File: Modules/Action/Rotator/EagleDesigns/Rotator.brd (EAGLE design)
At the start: 100 x 80 mm, 9 parts, among them U2 ATMEGA328P_TQFP

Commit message: Revert "Merge branch 'version-1.2'"
This reverts commit 982d9c85d5bd00c48b539e840003de48d3cf178d, reversing
changes made to b3895ae538c161df72313035d3e956c7a5ec4dbc.
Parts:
- removed C1, C2: 22pF, adafruit:C0603
- removed R2: 10K, resistor:R0603
- removed U$2: NX503, MakerWear:NX503
- removed U2: ATMEGA328P_TQFP, SparkFun-DigitalIC:TQFP32-08
- added U1: TINY85-20-DIP, SparkFun-DigitalIC:DIP08
- JP2: device SparkFun-Connectors:1X03 -> SparkFun-Connectors:1X04
- moved R1 14.8 mm to (4.58, 12.0), turned to 270 degrees
- moved JP3 3.74 mm to (20.7, 9.56), turned to 90 degrees
- moved JP1 1.66 mm to (17.2, 3.89)
- moved JP2 0.31 mm to (9.46, 20.2)
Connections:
- removed net 1X3SIN: U2.23
- removed net N$1: C1.1, U$2.P$1, U2.7
- removed net N$3: C2.1, U$2.P$2, U2.8
- removed net RESET: JP2.1, R2.1, U2.29
- removed net RX: JP2.2, U2.30
- removed net TX: JP2.3, U2.31
- new net MOSI: JP2.2, U1.5
- new net NRES: JP2.1, U1.1
- new net OUT(MISO): JP2.3, JP3.1, U1.6
- new net SCK: JP2.4, U1.7
- net 1X3SIN-SOUT: now also U1.2
- net GND: now also U1.4; no longer C1.2, C2.2, U2.21, U2.3, U2.5
- net VCC: now also U1.8; no longer R2.2, U2.18, U2.4, U2.6
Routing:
- net NRES: track 0.00 -> 22.7 mm
- net OUT(MISO): track 0.00 -> 20.6 mm
- net N$1: track 20.6 -> 0.00 mm, vias 1 -> 0
- net VCC: track 43.5 -> 23.4 mm, vias 1 -> 0
- net N$3: track 15.8 -> 0.00 mm, vias 1 -> 0
- net RESET: track 13.5 -> 0.00 mm
- net 1X3SIN-SOUT: track 14.4 -> 23.9 mm
- net SCK: track 0.00 -> 6.58 mm
- net GND: track 40.9 -> 34.5 mm, vias 1 -> 0
- net MOSI: track 0.00 -> 6.23 mm
- net TX: track 5.62 -> 0.00 mm
- net RX: track 3.94 -> 0.00 mm
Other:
- outline, holes or cut-outs redrawn
- board text added: "CTRL"
- board text added: "MISO"
- board text added: "MOSI"
- board text added: "MW-V3"
- board text added: "NRES"
- board text added: "SCK"
- board text added: "Servo Motor"
- board text added: "VCC"
- board text removed: "ROTATOR"

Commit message: added Rotator #30 eagle files
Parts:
- removed U1: TINY85-20-DIP, SparkFun-DigitalIC:DIP08
- added C1, C2: 22pF, adafruit:C0603
- added R2: 10K, resistor:R0603
- added U$2: NX503, MakerWear:NX503
- added U2: ATMEGA328P_TQFP, SparkFun-DigitalIC:TQFP32-08
- JP2: device SparkFun-Connectors:1X04 -> SparkFun-Connectors:1X03
- moved R1 14.8 mm to (17.7, 5.16), turned to 180 degrees
- moved JP3 3.74 mm to (19.9, 13.2), turned to 270 degrees
- moved JP1 1.66 mm to (16.0, 2.66)
- moved JP2 0.31 mm to (9.68, 20.4)
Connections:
- removed net MOSI: JP2.2, U1.5
- removed net NRES: JP2.1, U1.1
- removed net OUT(MISO): JP2.3, JP3.1, U1.6
- removed net SCK: JP2.4, U1.7
- new net 1X3SIN: U2.23
- new net N$1: C1.1, U$2.P$1, U2.7
- new net N$3: C2.1, U$2.P$2, U2.8
- new net RESET: JP2.1, R2.1, U2.29
- new net RX: JP2.2, U2.30
- new net TX: JP2.3, U2.31
- net 1X3SIN-SOUT: no longer U1.2
- net GND: now also C1.2, C2.2, U2.21, U2.3, U2.5; no longer U1.4
- net VCC: now also R2.2, U2.18, U2.4, U2.6; no longer U1.8
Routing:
- net NRES: track 22.7 -> 0.00 mm
- net OUT(MISO): track 20.6 -> 0.00 mm
- net N$1: track 0.00 -> 20.6 mm, vias 0 -> 1
- net VCC: track 23.4 -> 43.5 mm, vias 0 -> 1
- net N$3: track 0.00 -> 15.8 mm, vias 0 -> 1
- net RESET: track 0.00 -> 13.5 mm
- net 1X3SIN-SOUT: track 23.9 -> 14.4 mm
- net SCK: track 6.58 -> 0.00 mm
- net GND: track 34.5 -> 40.9 mm, vias 0 -> 1
- net MOSI: track 6.23 -> 0.00 mm
- net TX: track 0.00 -> 5.62 mm
- net RX: track 0.00 -> 3.94 mm
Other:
- outline, holes or cut-outs redrawn
- board text added: "ROTATOR"
- board text removed: "CTRL"
- board text removed: "MISO"
- board text removed: "MOSI"
- board text removed: "MW-V3"
- board text removed: "NRES"
- board text removed: "SCK"
- board text removed: "Servo Motor"
- board text removed: "VCC"

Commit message: fixed eagle files for new modules
SIN/SOUT was not correctly connected in them.
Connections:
- removed net 1X3SIN: U2.23
- new net SERVO: JP3.1, U2.13
- net 1X3SIN-SOUT: now also U2.23
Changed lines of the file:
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@@
 <wire x1="8.42" y1="4.02" x2="8.7" y2="4.3" width="0.3048" layer="1"/>
 <wire x1="8.7" y1="4.3" x2="15.8" y2="4.3" width="0.3048" layer="1"/>
+<contactref element="U2" pad="23"/>
+<wire x1="8.7" y1="4.3" x2="5.8074" y2="14.54" width="0" layer="19" extent="1-16"/>
 </signal>
 <signal name="RESET">
@@
 <wire x1="14.8" y1="20.15" x2="14.76" y2="20.39" width="0.3048" layer="16"/>
 </signal>
-<signal name="1X3SIN">
-<contactref element="U2" pad="23"/>
-</signal>
 <signal name="N$1">
 <contactref element="U$2" pad="P$1"/>
@@
 <wire x1="8" y1="12.03" x2="7.89" y2="15.04" width="0.3048" layer="1"/>
 </signal>
+<signal name="SERVO">
+<contactref element="U2" pad="13"/>
+<contactref element="JP3" pad="1"/>
+<wire x1="9.7" y1="8.2474" x2="19.89" y2="13.21" width="0" layer="19" extent="16-16"/>
+</signal>
 </signals>

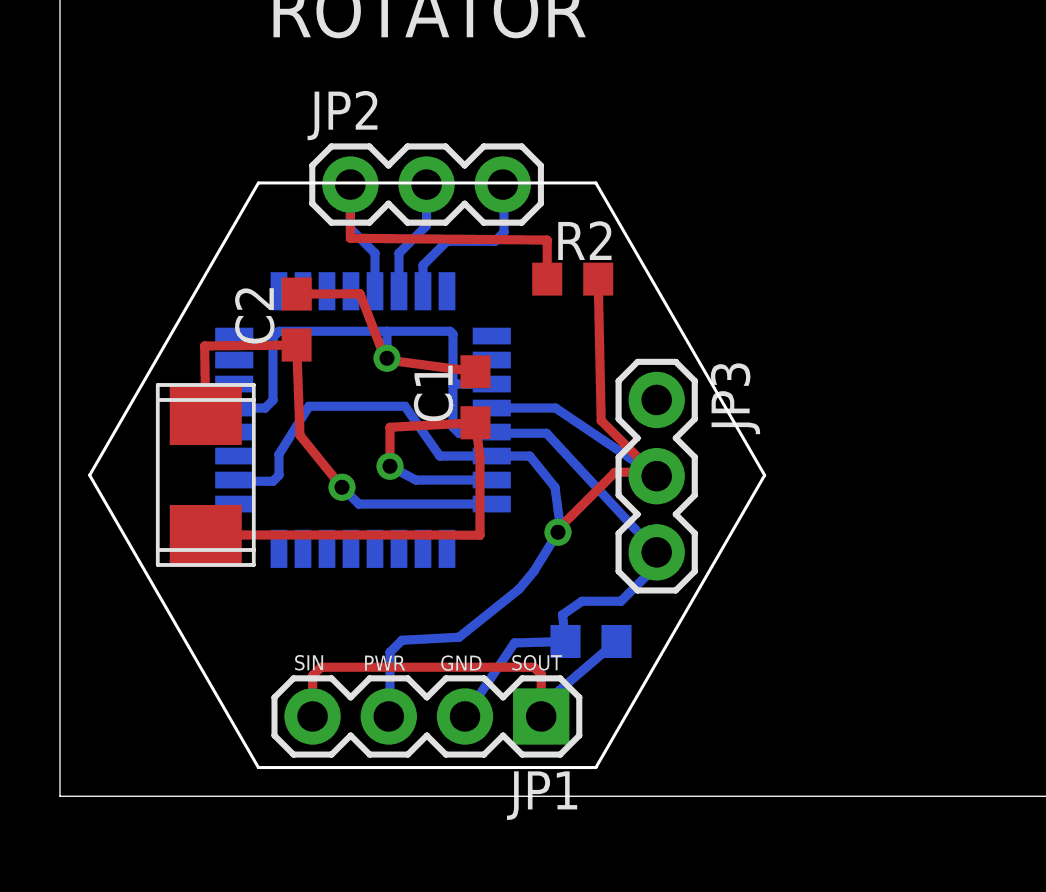
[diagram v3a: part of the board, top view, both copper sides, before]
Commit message: Rotator: added final PCB #30
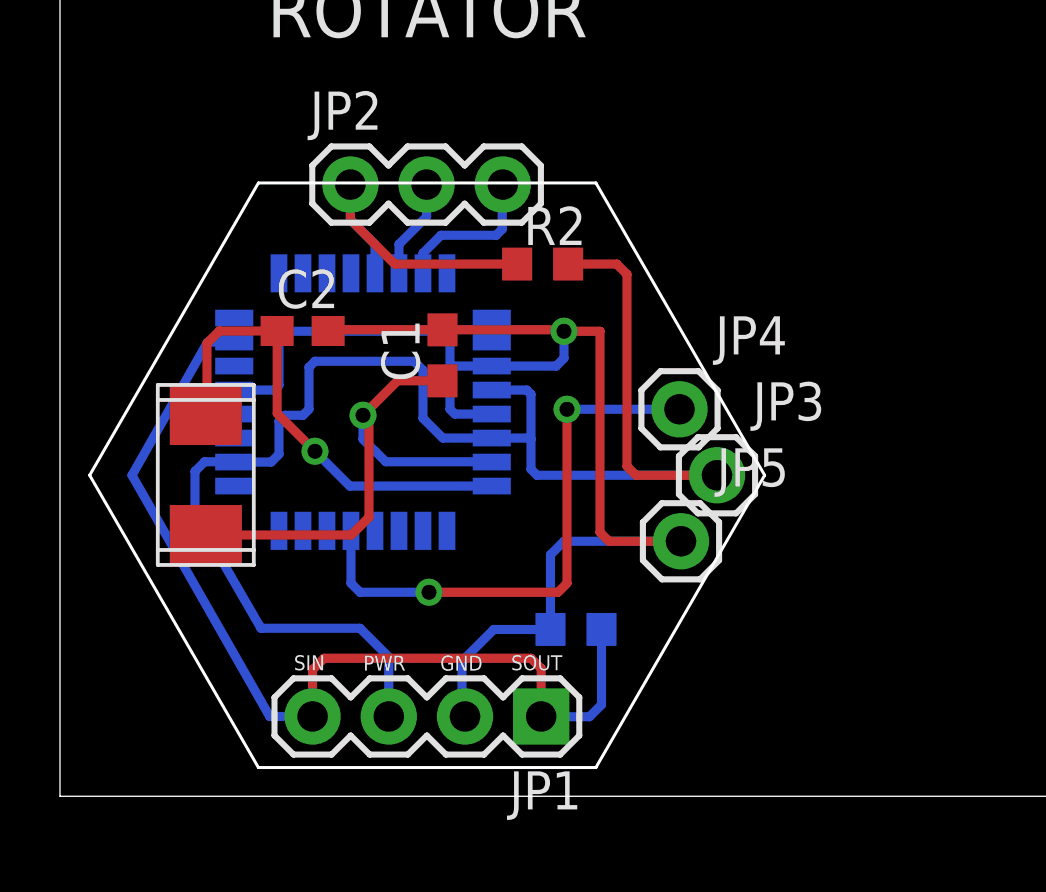
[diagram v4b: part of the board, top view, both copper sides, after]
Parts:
- added JP4, JP5: (no value), SparkFun-Connectors:1X01
- JP3: device SparkFun-Connectors:1X03 -> SparkFun-Connectors:1X01
- moved JP3 3.22 mm to (21.9, 10.7), turned to 0 degrees
- moved C1 1.78 mm to (12.8, 14.7)
- moved R2 1.12 mm to (16.1, 17.7)
- moved R1 0.64 mm to (17.2, 5.56)
- moved U2 0.60 mm to (10.1, 13.1)
- moved C2 0.43 mm to (8.09, 15.5), turned to 0 degrees
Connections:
- net GND: now also JP5.1; no longer JP3.3
- net SERVO: now also JP4.1; no longer JP3.1
- net VCC: now also JP3.1; no longer JP3.2
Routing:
- net SERVO: track 0.00 -> 18.7 mm, vias 0 -> 2
- net 1X3SIN-SOUT: track 14.4 -> 32.4 mm
- net GND: track 40.9 -> 48.5 mm
- net VCC: track 43.5 -> 50.4 mm, vias 1 -> 0
- net RESET: track 13.5 -> 10.6 mm
- net N$1: track 20.6 -> 17.7 mm
- net RX: track 3.94 -> 3.34 mm

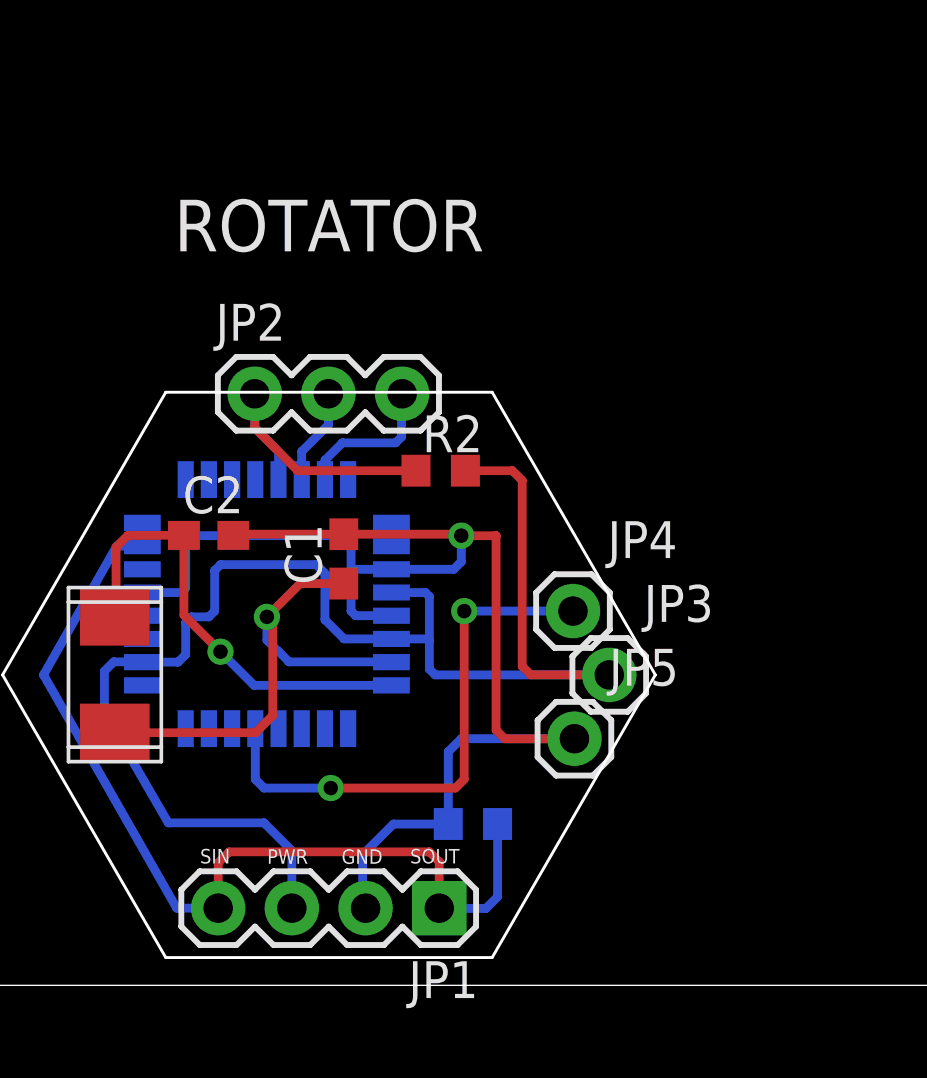
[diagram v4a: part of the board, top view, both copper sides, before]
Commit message: added version numbers, and deleted most of the text that was on each module.
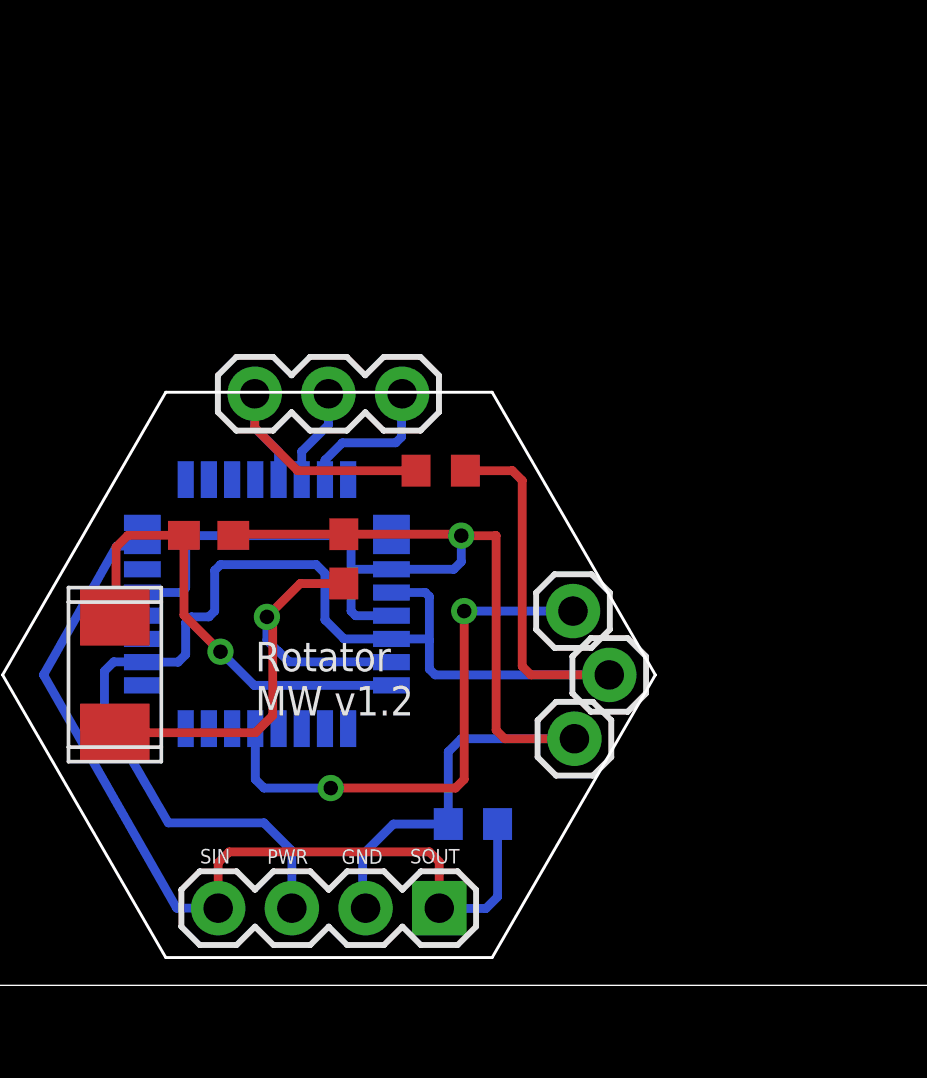
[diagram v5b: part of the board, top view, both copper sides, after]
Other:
- board text added: "Rotator MW v1.2"
- board text removed: "ROTATOR"
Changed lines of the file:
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@@
 <layer number="19" name="Unrouted" color="6" fill="1" visible="yes" active="yes"/>
 <layer number="20" name="Dimension" color="15" fill="1" visible="yes" active="yes"/>
-<layer number="21" name="tPlace" color="7" fill="1" visible="no" active="yes"/>
-<layer number="22" name="bPlace" color="7" fill="1" visible="no" active="yes"/>
+<layer number="21" name="tPlace" color="7" fill="1" visible="yes" active="yes"/>
+<layer number="22" name="bPlace" color="7" fill="1" visible="yes" active="yes"/>
 <layer number="23" name="tOrigins" color="15" fill="1" visible="yes" active="yes"/>
 <layer number="24" name="bOrigins" color="15" fill="1" visible="yes" active="yes"/>
-<layer number="25" name="tNames" color="7" fill="1" visible="no" active="yes"/>
-<layer number="26" name="bNames" color="7" fill="1" visible="no" active="yes"/>
-<layer number="27" name="tValues" color="7" fill="1" visible="no" active="yes"/>
-<layer number="28" name="bValues" color="7" fill="1" visible="no" active="yes"/>
+<layer number="25" name="tNames" color="7" fill="1" visible="yes" active="yes"/>
+<layer number="26" name="bNames" color="7" fill="1" visible="yes" active="yes"/>
+<layer number="27" name="tValues" color="7" fill="1" visible="yes" active="yes"/>
+<layer number="28" name="bValues" color="7" fill="1" visible="yes" active="yes"/>
 <layer number="29" name="tStop" color="7" fill="3" visible="no" active="yes"/>
 <layer number="30" name="bStop" color="7" fill="6" visible="no" active="yes"/>
@@
 <text x="12.6723" y="4.188" size="0.5" layer="21">GND</text>
 <text x="15.0345" y="4.2007" size="0.5" layer="21">SOUT</text>
-<text x="6.9" y="25.3" size="1.778" layer="21">ROTATOR</text>
+<text x="9.7" y="9.3" size="1.016" layer="21">Rotator
+MW v1.2</text>
 </plain>
 <attributes>
@@
 </autorouter>
 <elements>
-<element name="C1" library="adafruit" package="C0603" value="22pF" x="12.75" y="14.7" rot="R90"/>
-<element name="C2" library="adafruit" package="C0603" value="22pF" x="8.09" y="15.51"/>
-<element name="JP1" library="SparkFun-Connectors" package="1X04" value="" x="16.04" y="2.66" rot="R180"/>
-<element name="JP2" library="SparkFun-Connectors" package="1X03" value="" x="9.68" y="20.39"/>
-<element name="R1" library="adafruit" package="R0603" value="1M" x="17.2" y="5.56" rot="MR180"/>
-<element name="R2" library="resistor" package="R0603" value="10K" x="16.09" y="17.74"/>
-<element name="U$2" library="MakerWear" package="NX503" value="NX503" x="4.86" y="10.71" rot="R90"/>
-<element name="U2" library="SparkFun-DigitalIC" package="TQFP32-08" value="ATMEGA328P_TQFP" x="10.1" y="13.14" rot="MR0">
+<element name="C1" library="adafruit" package="C0603" value="22pF" x="12.75" y="14.7" smashed="yes" rot="R90"/>
+<element name="C2" library="adafruit" package="C0603" value="22pF" x="8.09" y="15.51" smashed="yes"/>
+<element name="JP1" library="SparkFun-Connectors" package="1X04" value="" x="16.04" y="2.66" smashed="yes" rot="R180">
+<attribute name="VALUE" x="17.31" y="5.835" size="1.27" layer="27" rot="R180"/>
+</element>
+<element name="JP2" library="SparkFun-Connectors" package="1X03" value="" x="9.68" y="20.39" smashed="yes">
+<attribute name="VALUE" x="8.41" y="17.215" size="1.27" layer="27"/>
+</element>
+<element name="R1" library="adafruit" package="R0603" value="1M" x="17.2" y="5.56" smashed="yes" rot="MR180"/>
+<element name="R2" library="resistor" package="R0603" value="10K" x="16.09" y="17.74" smashed="yes"/>
+<element name="U$2" library="MakerWear" package="NX503" value="NX503" x="4.86" y="10.71" smashed="yes" rot="R90"/>
+<element name="U2" library="SparkFun-DigitalIC" package="TQFP32-08" value="ATMEGA328P_TQFP" x="10.1" y="13.14" smashed="yes" rot="MR0">
 <attribute name="PROD_ID" value="IC-09069" x="10.1" y="13.14" size="1.778" layer="28" rot="MR0" display="off"/>
 </element>
-<element name="JP3" library="SparkFun-Connectors" package="1X01" value="" x="21.9" y="10.7"/>
-<element name="JP4" library="SparkFun-Connectors" package="1X01" value="" x="20.65" y="12.9"/>
-<element name="JP5" library="SparkFun-Connectors" package="1X01" value="" x="20.7" y="8.5"/>
+<element name="JP3" library="SparkFun-Connectors" package="1X01" value="" x="21.9" y="10.7" smashed="yes">
+<attribute name="VALUE" x="20.63" y="7.525" size="1.27" layer="27"/>
+</element>
+<element name="JP4" library="SparkFun-Connectors" package="1X01" value="" x="20.65" y="12.9" smashed="yes">
+<attribute name="VALUE" x="19.38" y="9.725" size="1.27" layer="27"/>
+</element>
+<element name="JP5" library="SparkFun-Connectors" package="1X01" value="" x="20.7" y="8.5" smashed="yes">
+<attribute name="VALUE" x="19.43" y="5.325" size="1.27" layer="27"/>
+</element>
 </elements>
 <signals>
@@
 </board>
 </drawing>
+<compatibility>
+<note version="6.3" minversion="6.2.2" severity="warning">
+Since Version 6.2.2 text objects can contain more than one line,
+which will not be processed correctly with this version.
+</note>
+</compatibility>
 </eagle>
